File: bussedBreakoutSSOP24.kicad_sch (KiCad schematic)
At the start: 45 parts, among them J1 Conn_01x12_Pin, J10 Conn_01x06_Pin, J11 Conn_01x06_Pin, J12 Conn_01x06_Pin, J13 Conn_01x06_Pin, J14 Conn_01x06_Pin, J15 Conn_01x06_Pin, J16 Conn_01x06_Pin, J17 Conn_01x06_Pin, J18 Conn_01x06_Pin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

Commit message: Change to a SSOP-24 0.65mm pitch breakout
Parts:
- J21: value SOP-24 -> SSOP-24; footprint SMD:SOP-24_3.9-7.5mmx15.4mm_P1.27mm -> SMD:SSOP-24_3.9-7.5mmx8.2mm_P0.65mm
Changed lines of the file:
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@@
 		)
 		(instances
-			(project "bussedBreakoutSOP24"
+			(project "bussedBreakoutSSOP24"
 				(path "/4df19105-13ee-4b1d-9e04-7651197a8529"
 					(reference "JP20")
@@
 		)
 		(instances
-			(project "bussedBreakoutSOP24"
+			(project "bussedBreakoutSSOP24"
 				(path "/4df19105-13ee-4b1d-9e04-7651197a8529"
 					(reference "J8")
@@
 		)
 		(instances
-			(project "bussedBreakoutSOP24"
+			(project "bussedBreakoutSSOP24"
 				(path "/4df19105-13ee-4b1d-9e04-7651197a8529"
 					(reference "JP21")
@@
 		)
 		(instances
-			(project "bussedBreakoutSOP24"
+			(project "bussedBreakoutSSOP24"
 				(path "/4df19105-13ee-4b1d-9e04-7651197a8529"
 					(reference "JP17")
@@
 		)
 		(instances
-			(project "bussedBreakoutSOP24"
+			(project "bussedBreakoutSSOP24"
 				(path "/4df19105-13ee-4b1d-9e04-7651197a8529"
 					(reference "JP18")
@@
 			)
 		)
-		(property "Value" "SOP-24"
+		(property "Value" "SSOP-24"
 			(at 105.41 19.05 0)
 			(effects
@@
 			)
 		)
-		(property "Footprint" "SMD:SOP-24_3.9-7.5mmx15.4mm_P1.27mm"
+		(property "Footprint" "SMD:SSOP-24_3.9-7.5mmx8.2mm_P0.65mm"
 			(at 104.14 35.56 0)
 			(effects
@@
 		)
 		(instances
-			(project "bussedBreakoutSOP24"
+			(project "bussedBreakoutSSOP24"
 				(path "/4df19105-13ee-4b1d-9e04-7651197a8529"
 					(reference "JP23")
@@
 		)
 		(instances
-			(project "bussedBreakoutSOP24"
+			(project "bussedBreakoutSSOP24"
 				(path "/4df19105-13ee-4b1d-9e04-7651197a8529"
 					(reference "JP24")
@@
 		)
 		(instances
-			(project "bussedBreakoutSOP24"
+			(project "bussedBreakoutSSOP24"
 				(path "/4df19105-13ee-4b1d-9e04-7651197a8529"
 					(reference "JP19")
@@
 		)
 		(instances
-			(project "bussedBreakoutSOP24"
+			(project "bussedBreakoutSSOP24"
 				(path "/4df19105-13ee-4b1d-9e04-7651197a8529"
 					(reference "JP22")

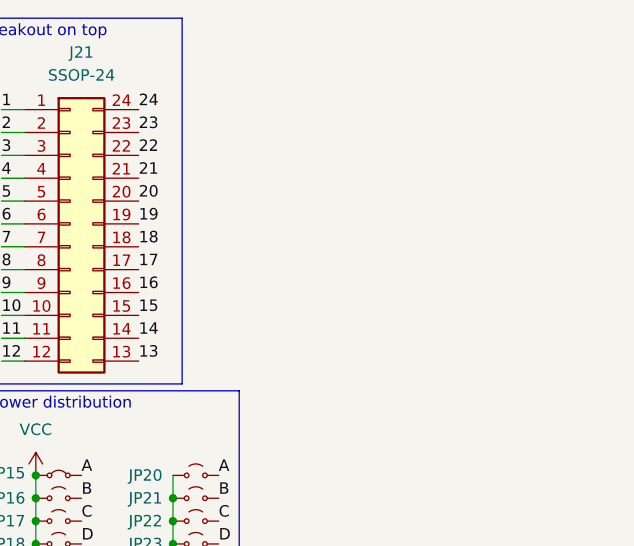
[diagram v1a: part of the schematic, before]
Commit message: Add some prototyping area on the top
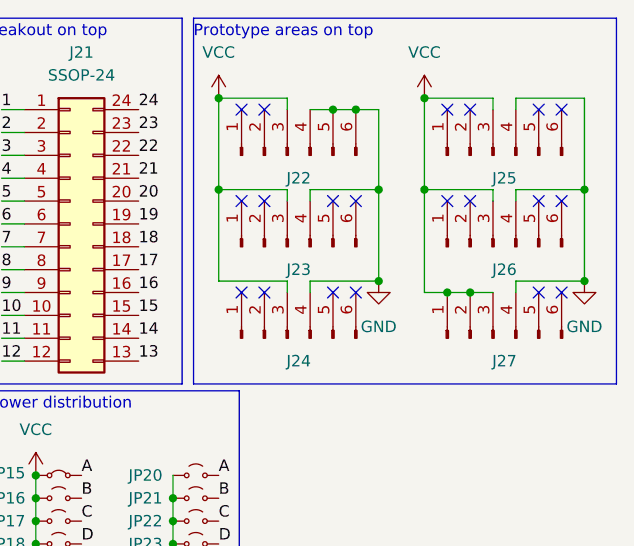
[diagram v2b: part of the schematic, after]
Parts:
- added J22, J23, J24, J25, J26, J27: Conn_01x06_Pin, SMD:SMD_0805_grid_1x6, symbol Connector:Conn_01x06_Pin
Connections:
- net GND: now also J22.4 (Pin_4), J22.5 (Pin_5), J22.6 (Pin_6), J23.4 (Pin_4), J24.4 (Pin_4), J25.4 (Pin_4), J26.4 (Pin_4), J27.4 (Pin_4)
- net VCC: now also J22.3 (Pin_3), J23.3 (Pin_3), J24.3 (Pin_3), J25.3 (Pin_3), J26.3 (Pin_3), J27.1 (Pin_1), J27.2 (Pin_2), J27.3 (Pin_3)
- no-connect marks 24 -> 44
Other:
- note added: "Prototype areas on top"
